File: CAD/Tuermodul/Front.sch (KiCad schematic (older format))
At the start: 45 parts, among them J301 Conn_02x20_Counter_Clockwise, Q301 Q_NPN_CBE, SW301 SW_SPDT_MSM, SW302 SW_SPDT_MSM, SW303 SW_SPDT_MSM, SW304 SW_SPDT_MSM

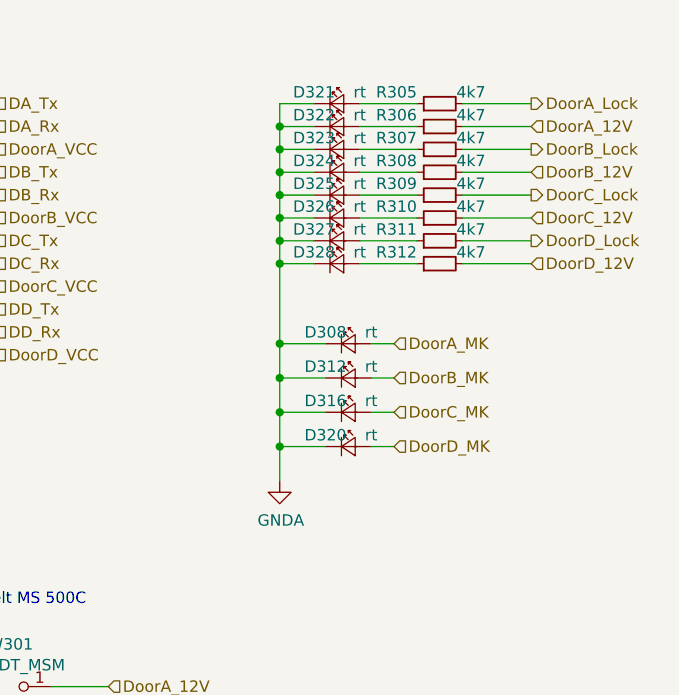
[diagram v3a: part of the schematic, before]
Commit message: -mod: Änderungen aus Review in Schaltplan und Layout
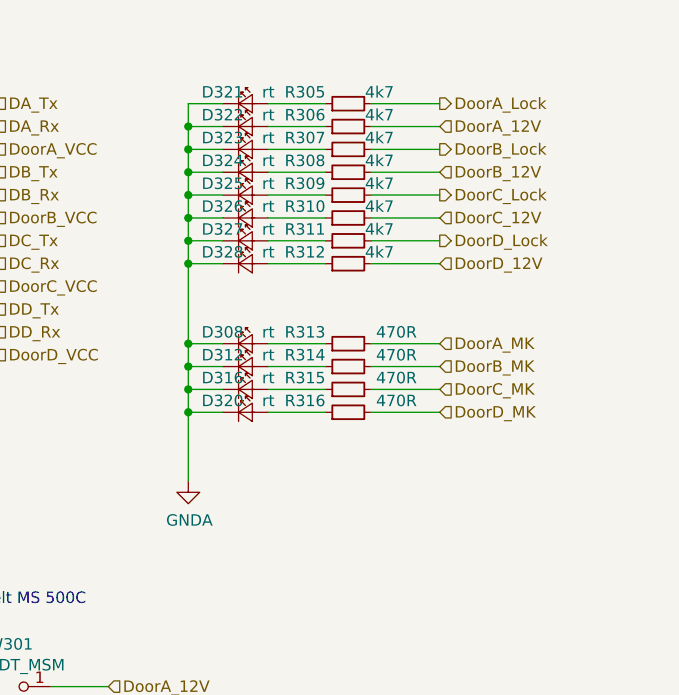
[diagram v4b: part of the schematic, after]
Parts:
- added R313, R314, R315, R316: 470R, Resistor_SMD:R_0603_1608Metric_Pad1.05x0.95mm_HandSolder, symbol Device:R_Small
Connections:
- net DoorA_MK: now also R313.2; no longer D308.2 (A)
- net DoorB_MK: now also R314.2; no longer D312.2 (A)
- net DoorC_MK: now also R315.2; no longer D316.2 (A)
- net DoorD_MK: now also R316.2; no longer D320.2 (A)
- new net: D308.2 (A), R313.1
- new net: D312.2 (A), R314.1
- new net: D316.2 (A), R315.1
- new net: D320.2 (A), R316.1
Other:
- moved on the sheet: D308, D312, D316, D320, D321, D322, D323, D324, D325, D326, D327, D328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

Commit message: -add: BOM -mod: letzte Schritte für LP Hersteller, Gerber Dateien für A0 generiert.
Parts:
- added R317, R318, R319, R320, R321, R322, R323, R324: 0, Resistor_SMD:R_0603_1608Metric_Pad1.05x0.95mm_HandSolder, symbol Device:R_Small
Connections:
- net GNDA: now also R317.2, R318.2, R319.2, R320.2, R321.2, R322.2, R323.2, R324.2
- new net GND: R317.1, R318.1, R319.1, R320.1, R321.1, R322.1, R323.1, R324.1
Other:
- note added: ""Connections""
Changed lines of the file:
@@
 Wire Wire Line
 	10100 2700 9850 2700
+$Comp
+L Device:R_Small R?
+U 1 1 5CA2B57E
+P 4600 4300
+AR Path="/5CA2B57E" Ref="R?"  Part="1"
+AR Path="/5C5BDAF5/5CA2B57E" Ref="R?"  Part="1"
+AR Path="/5C54653F/5CA2B57E" Ref="R317"  Part="1"
+F 0 "R317" V 4650 4400 50  0000 L CNN
+F 1 "0" V 4650 4100 50  0000 L CNN
+F 2 "Resistor_SMD:R_0603_1608Metric_Pad1.05x0.95mm_HandSolder" H 4600 4300 50  0001 C CNN
+F 3 "~" H 4600 4300 50  0001 C CNN
+	1    4600 4300
+	0    -1   -1   0
+$EndComp
+$Comp
+L Device:R_Small R?
+U 1 1 5CA2BB58
+P 4600 4450
+AR Path="/5CA2BB58" Ref="R?"  Part="1"
+AR Path="/5C5BDAF5/5CA2BB58" Ref="R?"  Part="1"
+AR Path="/5C54653F/5CA2BB58" Ref="R318"  Part="1"
+F 0 "R318" V 4650 4550 50  0000 L CNN
+F 1 "0" V 4650 4250 50  0000 L CNN
+F 2 "Resistor_SMD:R_0603_1608Metric_Pad1.05x0.95mm_HandSolder" H 4600 4450 50  0001 C CNN
+F 3 "~" H 4600 4450 50  0001 C CNN
+	1    4600 4450
+	0    -1   -1   0
+$EndComp
+$Comp
+L Device:R_Small R?
+U 1 1 5CA2BBD0
+P 4600 4600
+AR Path="/5CA2BBD0" Ref="R?"  Part="1"
+AR Path="/5C5BDAF5/5CA2BBD0" Ref="R?"  Part="1"
+AR Path="/5C54653F/5CA2BBD0" Ref="R319"  Part="1"
+F 0 "R319" V 4650 4700 50  0000 L CNN
+F 1 "0" V 4650 4400 50  0000 L CNN
+F 2 "Resistor_SMD:R_0603_1608Metric_Pad1.05x0.95mm_HandSolder" H 4600 4600 50  0001 C CNN
+F 3 "~" H 4600 4600 50  0001 C CNN
+	1    4600 4600
+	0    -1   -1   0
+$EndComp
+$Comp
+L Device:R_Small R?
+U 1 1 5CA2BC4A
+P 4600 4750
+AR Path="/5CA2BC4A" Ref="R?"  Part="1"
+AR Path="/5C5BDAF5/5CA2BC4A" Ref="R?"  Part="1"
+AR Path="/5C54653F/5CA2BC4A" Ref="R320"  Part="1"
+F 0 "R320" V 4650 4850 50  0000 L CNN
+F 1 "0" V 4650 4550 50  0000 L CNN
+F 2 "Resistor_SMD:R_0603_1608Metric_Pad1.05x0.95mm_HandSolder" H 4600 4750 50  0001 C CNN
+F 3 "~" H 4600 4750 50  0001 C CNN
+	1    4600 4750
+	0    -1   -1   0
+$EndComp
+$Comp
+L Device:R_Small R?
+U 1 1 5CA2BCC6
+P 4600 4900
+AR Path="/5CA2BCC6" Ref="R?"  Part="1"
+AR Path="/5C5BDAF5/5CA2BCC6" Ref="R?"  Part="1"
+AR Path="/5C54653F/5CA2BCC6" Ref="R321"  Part="1"
+F 0 "R321" V 4650 5000 50  0000 L CNN
+F 1 "0" V 4650 4700 50  0000 L CNN
+F 2 "Resistor_SMD:R_0603_1608Metric_Pad1.05x0.95mm_HandSolder" H 4600 4900 50  0001 C CNN
+F 3 "~" H 4600 4900 50  0001 C CNN
+	1    4600 4900
+	0    -1   -1   0
+$EndComp
+$Comp
+L Device:R_Small R?
+U 1 1 5CA2BD56
+P 4600 5050
+AR Path="/5CA2BD56" Ref="R?"  Part="1"
+AR Path="/5C5BDAF5/5CA2BD56" Ref="R?"  Part="1"
+AR Path="/5C54653F/5CA2BD56" Ref="R322"  Part="1"
+F 0 "R322" V 4650 5150 50  0000 L CNN
+F 1 "0" V 4650 4850 50  0000 L CNN
+F 2 "Resistor_SMD:R_0603_1608Metric_Pad1.05x0.95mm_HandSolder" H 4600 5050 50  0001 C CNN
+F 3 "~" H 4600 5050 50  0001 C CNN
+	1    4600 5050
+	0    -1   -1   0
+$EndComp
+$Comp
+L Device:R_Small R?
+U 1 1 5CA2BDDE
+P 4600 5200
+AR Path="/5CA2BDDE" Ref="R?"  Part="1"
+AR Path="/5C5BDAF5/5CA2BDDE" Ref="R?"  Part="1"
+AR Path="/5C54653F/5CA2BDDE" Ref="R323"  Part="1"
+F 0 "R323" V 4650 5300 50  0000 L CNN
+F 1 "0" V 4650 5000 50  0000 L CNN
+F 2 "Resistor_SMD:R_0603_1608Metric_Pad1.05x0.95mm_HandSolder" H 4600 5200 50  0001 C CNN
+F 3 "~" H 4600 5200 50  0001 C CNN
+	1    4600 5200
+	0    -1   -1   0
+$EndComp
+$Comp
+L Device:R_Small R?
+U 1 1 5CA2BED0
+P 4600 5350
+AR Path="/5CA2BED0" Ref="R?"  Part="1"
+AR Path="/5C5BDAF5/5CA2BED0" Ref="R?"  Part="1"
+AR Path="/5C54653F/5CA2BED0" Ref="R324"  Part="1"
+F 0 "R324" V 4650 5450 50  0000 L CNN
+F 1 "0" V 4650 5150 50  0000 L CNN
+F 2 "Resistor_SMD:R_0603_1608Metric_Pad1.05x0.95mm_HandSolder" H 4600 5350 50  0001 C CNN
+F 3 "~" H 4600 5350 50  0001 C CNN
+	1    4600 5350
+	0    -1   -1   0
+$EndComp
+$Comp
+L power:GNDA #PWR0146
+U 1 1 5CA2BF64
+P 4850 5450
+F 0 "#PWR0146" H 4850 5200 50  0001 C CNN
+F 1 "GNDA" V 4855 5323 50  0000 R CNN
+F 2 "" H 4850 5450 50  0001 C CNN
+F 3 "" H 4850 5450 50  0001 C CNN
+	1    4850 5450
+	1    0    0    -1
+$EndComp
+$Comp
+L power:GND #PWR?
+U 1 1 5CA4583E
+P 4350 5450
+AR Path="/5CA4583E" Ref="#PWR?"  Part="1"
+AR Path="/5C54653F/5CA4583E" Ref="#PWR0147"  Part="1"
+F 0 "#PWR0147" H 4350 5200 50  0001 C CNN
+F 1 "GND" H 4355 5277 50  0000 C CNN
+F 2 "" H 4350 5450 50  0001 C CNN
+F 3 "" H 4350 5450 50  0001 C CNN
+	1    4350 5450
+	1    0    0    -1
+$EndComp
+Wire Wire Line
+	4700 5350 4850 5350
+Wire Wire Line
+	4850 5350 4850 5450
+Wire Wire Line
+	4500 5350 4350 5350
+Wire Wire Line
+	4350 5350 4350 5450
+Wire Wire Line
+	4700 5200 4850 5200
+Wire Wire Line
+	4850 5200 4850 5350
+Connection ~ 4850 5350
+Wire Wire Line
+	4700 5050 4850 5050
+Wire Wire Line
+	4850 5050 4850 5200
+Connection ~ 4850 5200
+Wire Wire Line
+	4700 4900 4850 4900
+Wire Wire Line
+	4850 4900 4850 5050
+Connection ~ 4850 5050
+Wire Wire Line
+	4700 4750 4850 4750
+Wire Wire Line
+	4850 4750 4850 4900
+Connection ~ 4850 4900
+Wire Wire Line
+	4700 4600 4850 4600
+Wire Wire Line
+	4850 4600 4850 4750
+Connection ~ 4850 4750
+Wire Wire Line
+	4700 4300 4850 4300
+Wire Wire Line
+	4850 4300 4850 4450
+Connection ~ 4850 4600
+Wire Wire Line
+	4700 4450 4850 4450
+Connection ~ 4850 4450
+Wire Wire Line
+	4850 4450 4850 4600
+Wire Wire Line
+	4500 4300 4350 4300
+Wire Wire Line
+	4350 4300 4350 4450
+Connection ~ 4350 5350
+Wire Wire Line
+	4500 5200 4350 5200
+Connection ~ 4350 5200
+Wire Wire Line
+	4350 5200 4350 5350
+Wire Wire Line
+	4500 5050 4350 5050
+Connection ~ 4350 5050
+Wire Wire Line
+	4350 5050 4350 5200
+Wire Wire Line
+	4500 4450 4350 4450
+Connection ~ 4350 4450
+Wire Wire Line
+	4350 4450 4350 4600
+Wire Wire Line
+	4500 4600 4350 4600
+Connection ~ 4350 4600
+Wire Wire Line
+	4350 4600 4350 4750
+Wire Wire Line
+	4500 4750 4350 4750
+Connection ~ 4350 4750
+Wire Wire Line
+	4350 4750 4350 4900
+Wire Wire Line
+	4500 4900 4350 4900
+Connection ~ 4350 4900
+Wire Wire Line
+	4350 4900 4350 5050
+Text Notes 4350 4150 0    50   ~ 0
+"Connections"
 $EndSCHEMATC
